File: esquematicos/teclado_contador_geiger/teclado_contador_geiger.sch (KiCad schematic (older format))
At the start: 14 parts, among them J1 Conn_01x04_Female, SW1 SW_SPST, SW2 SW_SPST, SW3 SW_SPST, SW4 SW_SPST, SW5 SW_SPST, SW6 SW_SPST

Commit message: Agregado del PCB del teclado(2)
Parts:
- J1: footprint Connector_JST:JST_EH_B04B-EH-A_1x04_P2.50mm_Vertical -> Connector_JST:JST_XH_B04B-XH-A_1x04_P2.50mm_Vertical
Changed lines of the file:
@@
 EESchema Schematic File Version 4
+LIBS:teclado_contador_geiger-cache
 EELAYER 26 0
 EELAYER END
@@
 F 0 "J1" H 4327 1726 50  0000 L CNN
 F 1 "Conn_01x04_Female" H 4327 1635 50  0000 L CNN
-F 2 "Connector_JST:JST_EH_B04B-EH-A_1x04_P2.50mm_Vertical" H 4300 1750 50  0001 C CNN
+F 2 "Connector_JST:JST_XH_B04B-XH-A_1x04_P2.50mm_Vertical" H 4300 1750 50  0001 C CNN
 F 3 "~" H 4300 1750 50  0001 C CNN
 	1    4300 1750

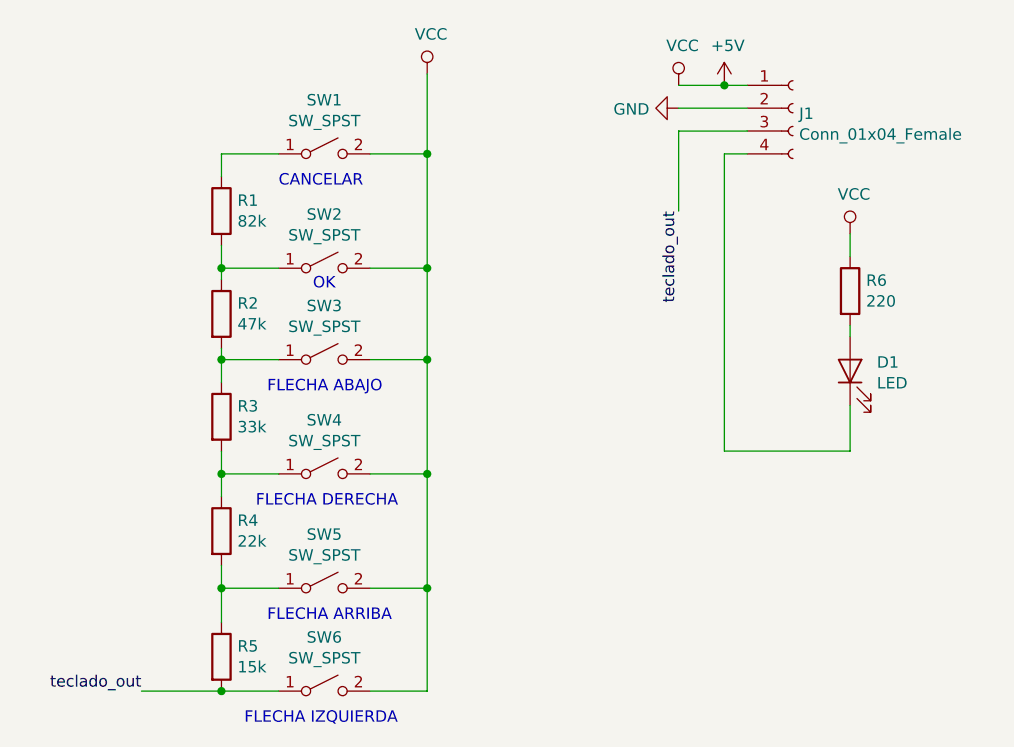
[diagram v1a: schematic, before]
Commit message: Agregado de LED verde a la placa del teclado e incremento de las dimensiones de esta última incluyendo una mayor separación entre los botones
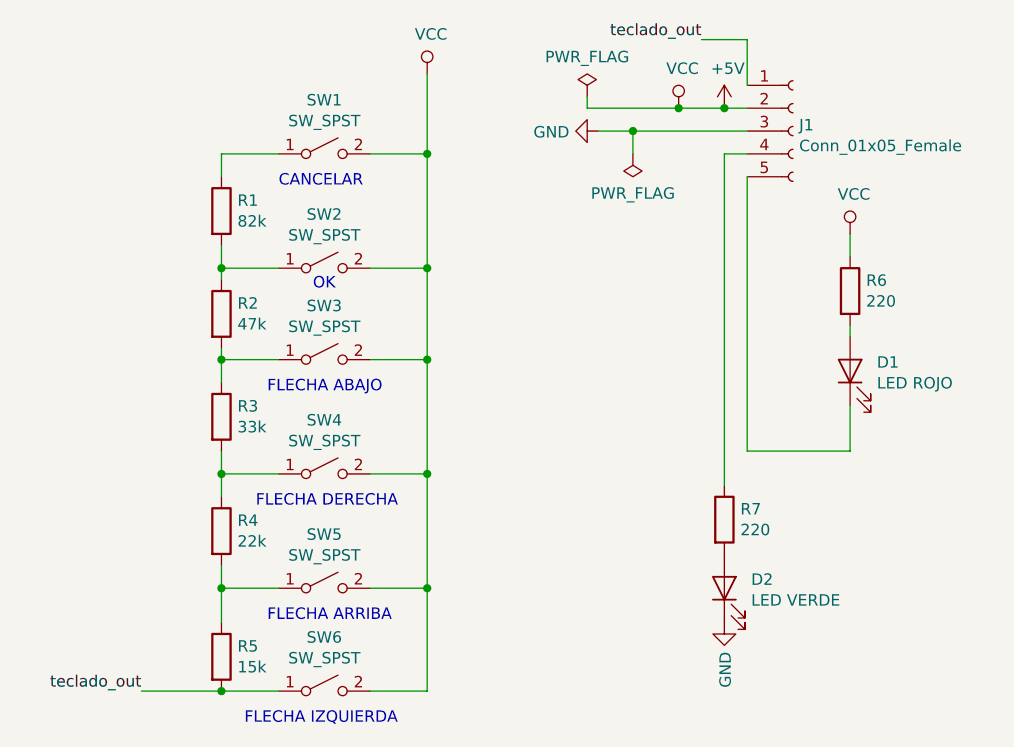
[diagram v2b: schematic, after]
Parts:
- removed J1: Conn_01x04_Female, Connector_JST:JST_XH_B04B-XH-A_1x04_P2.50mm_Vertical, symbol Connector:Conn_01x04_Female
- added D2: LED VERDE, LED_THT:LED_D5.0mm, symbol Device:LED
- added J1: Conn_01x05_Female, Connector_JST:JST_XH_B05B-XH-A_1x05_P2.50mm_Vertical, symbol Connector:Conn_01x05_Female
- added R7: 220, Resistor_SMD:R_0805_2012Metric_Pad1.15x1.40mm_HandSolder, symbol Device:R
- D1: value LED -> LED ROJO
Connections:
- net +5V: now also J1.2 (Pin_2)
- net GND: now also D2.1 (K), J1.3 (Pin_3)
- net teclado_out: now also J1.1 (Pin_1)
- net at D1.1 (K): now also J1.5 (Pin_5)
- new net: J1.4 (Pin_4), R7.1
- new net: D2.2 (A), R7.2
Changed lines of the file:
@@
 	1    0    0    -1
 $EndComp
-Wire Wire Line
-	4100 1650 4000 1650
 $Comp
 L power:VCC #PWR02
 U 1 1 5D5878D8
-P 3800 1650
-F 0 "#PWR02" H 3800 1500 50  0001 C CNN
-F 1 "VCC" H 3817 1823 50  0000 C CNN
-F 2 "" H 3800 1650 50  0001 C CNN
-F 3 "" H 3800 1650 50  0001 C CNN
-	1    3800 1650
+P 3800 1750
+F 0 "#PWR02" H 3800 1600 50  0001 C CNN
+F 1 "VCC" H 3817 1923 50  0000 C CNN
+F 2 "" H 3800 1750 50  0001 C CNN
+F 3 "" H 3800 1750 50  0001 C CNN
+	1    3800 1750
 	1    0    0    -1
 $EndComp
@@
 L power:+5V #PWR04
 U 1 1 5D58793E
-P 4000 1650
-F 0 "#PWR04" H 4000 1500 50  0001 C CNN
-F 1 "+5V" H 4015 1823 50  0000 C CNN
-F 2 "" H 4000 1650 50  0001 C CNN
-F 3 "" H 4000 1650 50  0001 C CNN
-	1    4000 1650
-	1    0    0    -1
-$EndComp
-Connection ~ 4000 1650
-Wire Wire Line
-	4000 1650 3800 1650
+P 4000 1750
+F 0 "#PWR04" H 4000 1600 50  0001 C CNN
+F 1 "+5V" H 4015 1923 50  0000 C CNN
+F 2 "" H 4000 1750 50  0001 C CNN
+F 3 "" H 4000 1750 50  0001 C CNN
+	1    4000 1750
+	1    0    0    -1
+$EndComp
+Wire Wire Line
+	4000 1750 3800 1750
 Wire Wire Line
 	1800 2350 1800 2450
 Wire Wire Line
 	1800 3250 1800 3350
-$Comp
-L Connector:Conn_01x04_Female J1
-U 1 1 5D58773D
-P 4300 1750
-F 0 "J1" H 4327 1726 50  0000 L CNN
-F 1 "Conn_01x04_Female" H 4327 1635 50  0000 L CNN
-F 2 "Connector_JST:JST_XH_B04B-XH-A_1x04_P2.50mm_Vertical" H 4300 1750 50  0001 C CNN
-F 3 "~" H 4300 1750 50  0001 C CNN
-	1    4300 1750
-	1    0    0    -1
-$EndComp
 $Comp
 L Device:R R5
@@
 L power:GND #PWR03
 U 1 1 5D5892F1
-P 3800 1750
-F 0 "#PWR03" H 3800 1500 50  0001 C CNN
-F 1 "GND" V 3805 1622 50  0000 R CNN
-F 2 "" H 3800 1750 50  0001 C CNN
-F 3 "" H 3800 1750 50  0001 C CNN
-	1    3800 1750
+P 3450 1850
+F 0 "#PWR03" H 3450 1600 50  0001 C CNN
+F 1 "GND" V 3455 1722 50  0000 R CNN
+F 2 "" H 3450 1850 50  0001 C CNN
+F 3 "" H 3450 1850 50  0001 C CNN
+	1    3450 1850
 	0    1    1    0
 $EndComp
 Wire Wire Line
-	3800 1750 4100 1750
+	3450 1850 3600 1850
 Text Label 1450 4300 2    50   ~ 0
 teclado_out
@@
 Wire Wire Line
 	1800 4300 2050 4300
-Text Label 3800 2200 3    50   ~ 0
+Text Label 3900 1450 2    50   ~ 0
 teclado_out
-Wire Wire Line
-	3800 2200 3800 1850
-Wire Wire Line
-	3800 1850 4100 1850
 $Comp
 L Device:LED D1
@@
 P 4550 2900
 F 0 "D1" V 4588 2783 50  0000 R CNN
-F 1 "LED" V 4497 2783 50  0000 R CNN
+F 1 "LED ROJO" V 4497 2783 50  0000 R CNN
 F 2 "LED_THT:LED_D5.0mm" H 4550 2900 50  0001 C CNN
 F 3 "~" H 4550 2900 50  0001 C CNN
@@
 Wire Wire Line
 	4550 2300 4550 2400
-Wire Wire Line
-	4550 3250 4000 3250
-Wire Wire Line
-	4000 3250 4000 1950
-Wire Wire Line
-	4000 1950 4100 1950
 Wire Wire Line
 	4550 3050 4550 3250
@@
 Text Notes 1900 4450 0    50   ~ 0
 FLECHA IZQUIERDA\n
+$Comp
+L Connector:Conn_01x05_Female J1
+U 1 1 5D5FED87
+P 4300 1850
+F 0 "J1" H 4327 1876 50  0000 L CNN
+F 1 "Conn_01x05_Female" H 4327 1785 50  0000 L CNN
+F 2 "Connector_JST:JST_XH_B05B-XH-A_1x05_P2.50mm_Vertical" H 4300 1850 50  0001 C CNN
+F 3 "~" H 4300 1850 50  0001 C CNN
+	1    4300 1850
+	1    0    0    -1
+$EndComp
+Wire Wire Line
+	4100 2050 4100 3250
+Wire Wire Line
+	4100 3250 4550 3250
+$Comp
+L Device:R R7
+U 1 1 5D5FF6D2
+P 4000 3550
+F 0 "R7" H 4070 3596 50  0000 L CNN
+F 1 "220" H 4070 3505 50  0000 L CNN
+F 2 "Resistor_SMD:R_0805_2012Metric_Pad1.15x1.40mm_HandSolder" V 3930 3550 50  0001 C CNN
+F 3 "~" H 4000 3550 50  0001 C CNN
+	1    4000 3550
+	1    0    0    -1
+$EndComp
+$Comp
+L Device:LED D2
+U 1 1 5D5FF722
+P 4000 3850
+F 0 "D2" V 4038 3733 50  0000 R CNN
+F 1 "LED VERDE" V 3947 3733 50  0000 R CNN
+F 2 "LED_THT:LED_D5.0mm" H 4000 3850 50  0001 C CNN
+F 3 "~" H 4000 3850 50  0001 C CNN
+	1    4000 3850
+	0    -1   -1   0
+$EndComp
+Wire Wire Line
+	4100 1950 4000 1950
+Wire Wire Line
+	4000 1950 4000 3400
+$Comp
+L power:GND #PWR06
+U 1 1 5D600919
+P 4000 4000
+F 0 "#PWR06" H 4000 3750 50  0001 C CNN
+F 1 "GND" V 4005 3872 50  0000 R CNN
+F 2 "" H 4000 4000 50  0001 C CNN
+F 3 "" H 4000 4000 50  0001 C CNN
+	1    4000 4000
+	1    0    0    -1
+$EndComp
+$Comp
+L power:PWR_FLAG #FLG0101
+U 1 1 5D600B09
+P 3400 1700
+F 0 "#FLG0101" H 3400 1775 50  0001 C CNN
+F 1 "PWR_FLAG" H 3400 1874 50  0000 C CNN
+F 2 "" H 3400 1700 50  0001 C CNN
+F 3 "~" H 3400 1700 50  0001 C CNN
+	1    3400 1700
+	1    0    0    -1
+$EndComp
+Wire Wire Line
+	3400 1700 3400 1750
+Wire Wire Line
+	3400 1750 3800 1750
+Connection ~ 3800 1750
+$Comp
+L power:PWR_FLAG #FLG0102
+U 1 1 5D6018ED
+P 3600 1950
+F 0 "#FLG0102" H 3600 2025 50  0001 C CNN
+F 1 "PWR_FLAG" H 3600 2123 50  0000 C CNN
+F 2 "" H 3600 1950 50  0001 C CNN
+F 3 "~" H 3600 1950 50  0001 C CNN
+	1    3600 1950
+	-1   0    0    1
+$EndComp
+Wire Wire Line
+	3600 1850 3600 1950
+Wire Wire Line
+	3600 1850 4100 1850
+Connection ~ 3600 1850
+Wire Wire Line
+	4000 1750 4100 1750
+Connection ~ 4000 1750
+Wire Wire Line
+	3900 1450 4100 1450
+Wire Wire Line
+	4100 1450 4100 1650
 $EndSCHEMATC

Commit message: Agrega PCB del teclado
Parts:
- J1: footprint Connector_JST:JST_XH_B05B-XH-A_1x05_P2.50mm_Vertical -> Connectors_Molex:Molex_KK-6410-05_05x2.54mm_Straight
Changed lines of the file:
@@
 F 0 "J1" H 4327 1876 50  0000 L CNN
 F 1 "Conn_01x05_Female" H 4327 1785 50  0000 L CNN
-F 2 "Connector_JST:JST_XH_B05B-XH-A_1x05_P2.50mm_Vertical" H 4300 1850 50  0001 C CNN
+F 2 "Connectors_Molex:Molex_KK-6410-05_05x2.54mm_Straight" H 4300 1850 50  0001 C CNN
 F 3 "~" H 4300 1850 50  0001 C CNN
 	1    4300 1850
